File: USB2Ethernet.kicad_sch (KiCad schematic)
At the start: 23 parts, among them U15 LAN9512, U17 CAT250xxx, Y5 25Mhz

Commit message: change cad data
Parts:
- added C102, C97: 0.1uF, Capacitor_SMD:C_0402_1005Metric_Pad0.74x0.62mm_HandSolder, symbol Device:C
- added FB4: FerriteBead, Inductor_SMD:L_0603_1608Metric_Pad1.05x0.95mm_HandSolder, symbol Device:FerriteBead
- added R54, R55, R56, R57: 49.9Ω, Resistor_SMD:R_0603_1608Metric_Pad0.98x0.95mm_HandSolder, symbol Device:R
- added R59, R61: 12kΩ, Resistor_SMD:R_0603_1608Metric_Pad0.98x0.95mm_HandSolder, symbol Device:R
- added R63: 1k, Resistor_SMD:R_0603_1608Metric_Pad0.98x0.95mm_HandSolder, symbol Device:R
- R64: renamed from R46; value 320kΩ -> 10kΩ
- Y6: renamed from Y5; footprint Crystal:Crystal_SMD_SeikoEpson_FA238-4Pin_3.2x2.5mm -> Crystal:Crystal_SMD_SeikoEpson_FA128-4Pin_2.0x1.6mm
- renumbered C84 to C111, C86 to C112, C92 to C113, C93 to C122, C98 to C123, C99 to C124, C100 to C128, C105 to C129, C109 to C131, C110 to C132, C112 to C134, C64 to C86, C69 to C88, C72 to C92, C73 to C93, C71 to C94, C70 to C95, C68 to C96, FB2 to FB5, U15 to U16, U17 to U18
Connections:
- net +3.3V: now also U16.41 (AUTOMDIX_EN), R54.1, R55.1, R56.1, R57.1, R63.1
- net 1.8V: no longer U16.48 (VDD18ETHPLL)
- net GND: now also R59.1, R61.1
- net RXN: now also R54.2
- net RXP: now also R55.2
- net TXN: now also R56.2
- net TXP: now also R57.2
- net at U16.62 (VDD18USBPLL): now also C97.2
- net at U16.11 (VBUS_DET): now also R63.2
- net USB2DM: now reaches U16.3 (USBDM3)
- net USB2DP: now reaches U16.4 (USBDP3)
- net at U16.50 (EXRES): now also R59.2
- net at U16.63 (USBRBIAS): now also R61.2
- new net: C102.2, U16.48 (VDD18ETHPLL)
- new net: C102.1, FB4.1
- new net: C97.1, FB4.2
- no-connect marks 0 -> 12
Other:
- moved on the sheet: C111, C112, C113, C122, C123, C124, C128, C129, C131, C132, C134, C86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

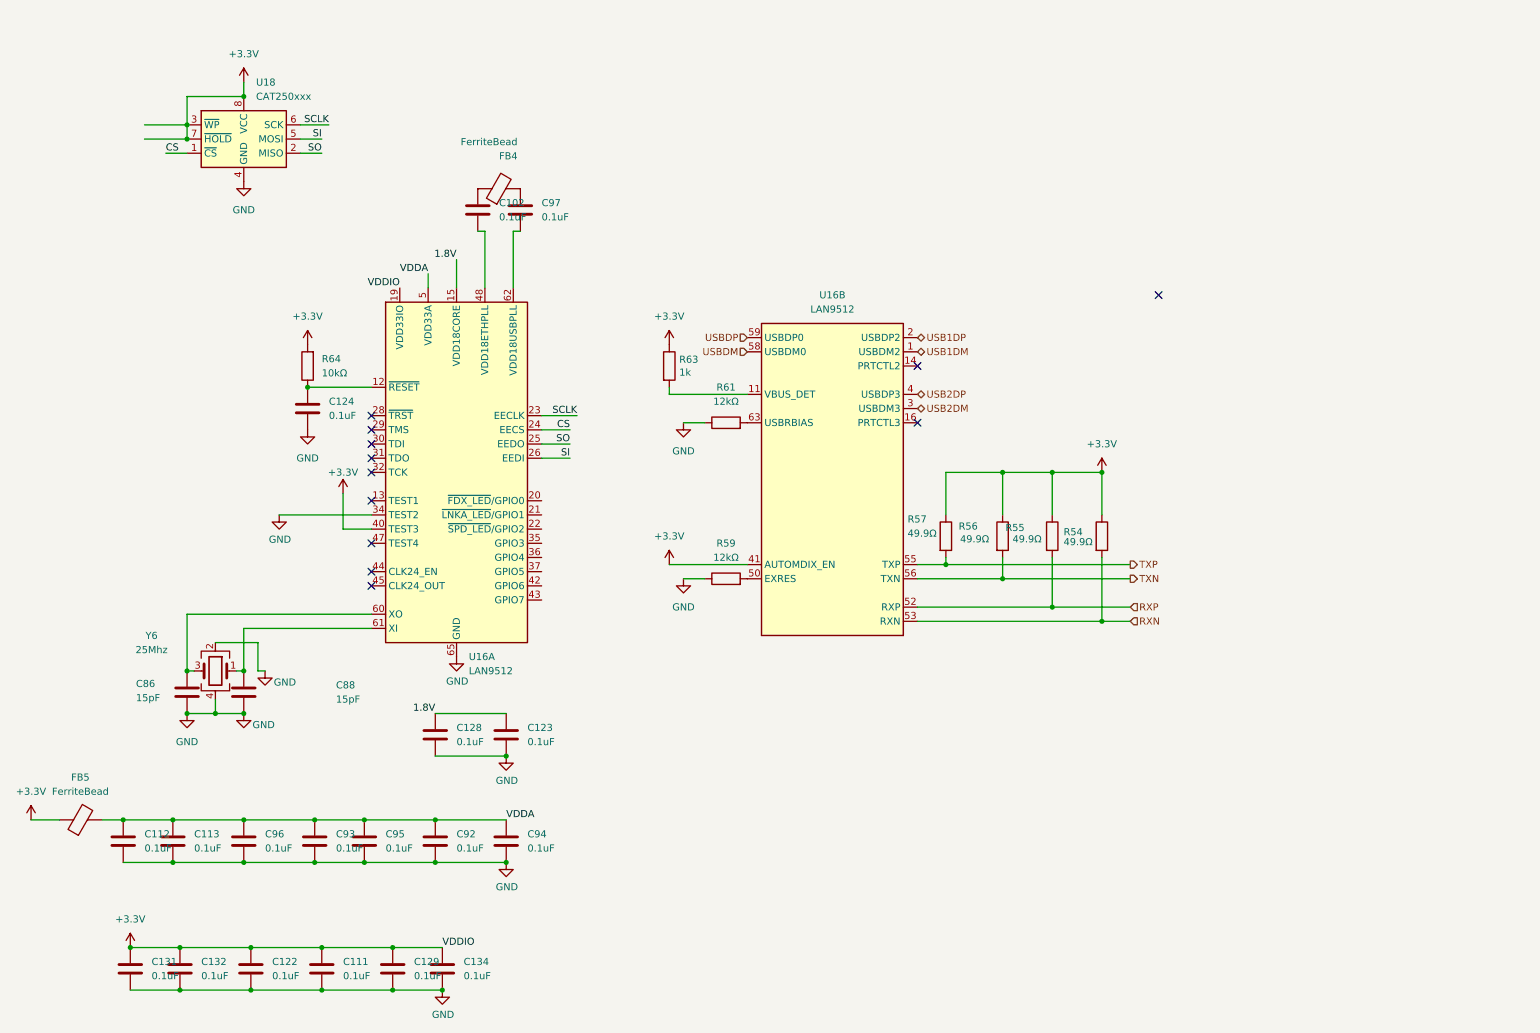
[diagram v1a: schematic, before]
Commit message: remove efuse
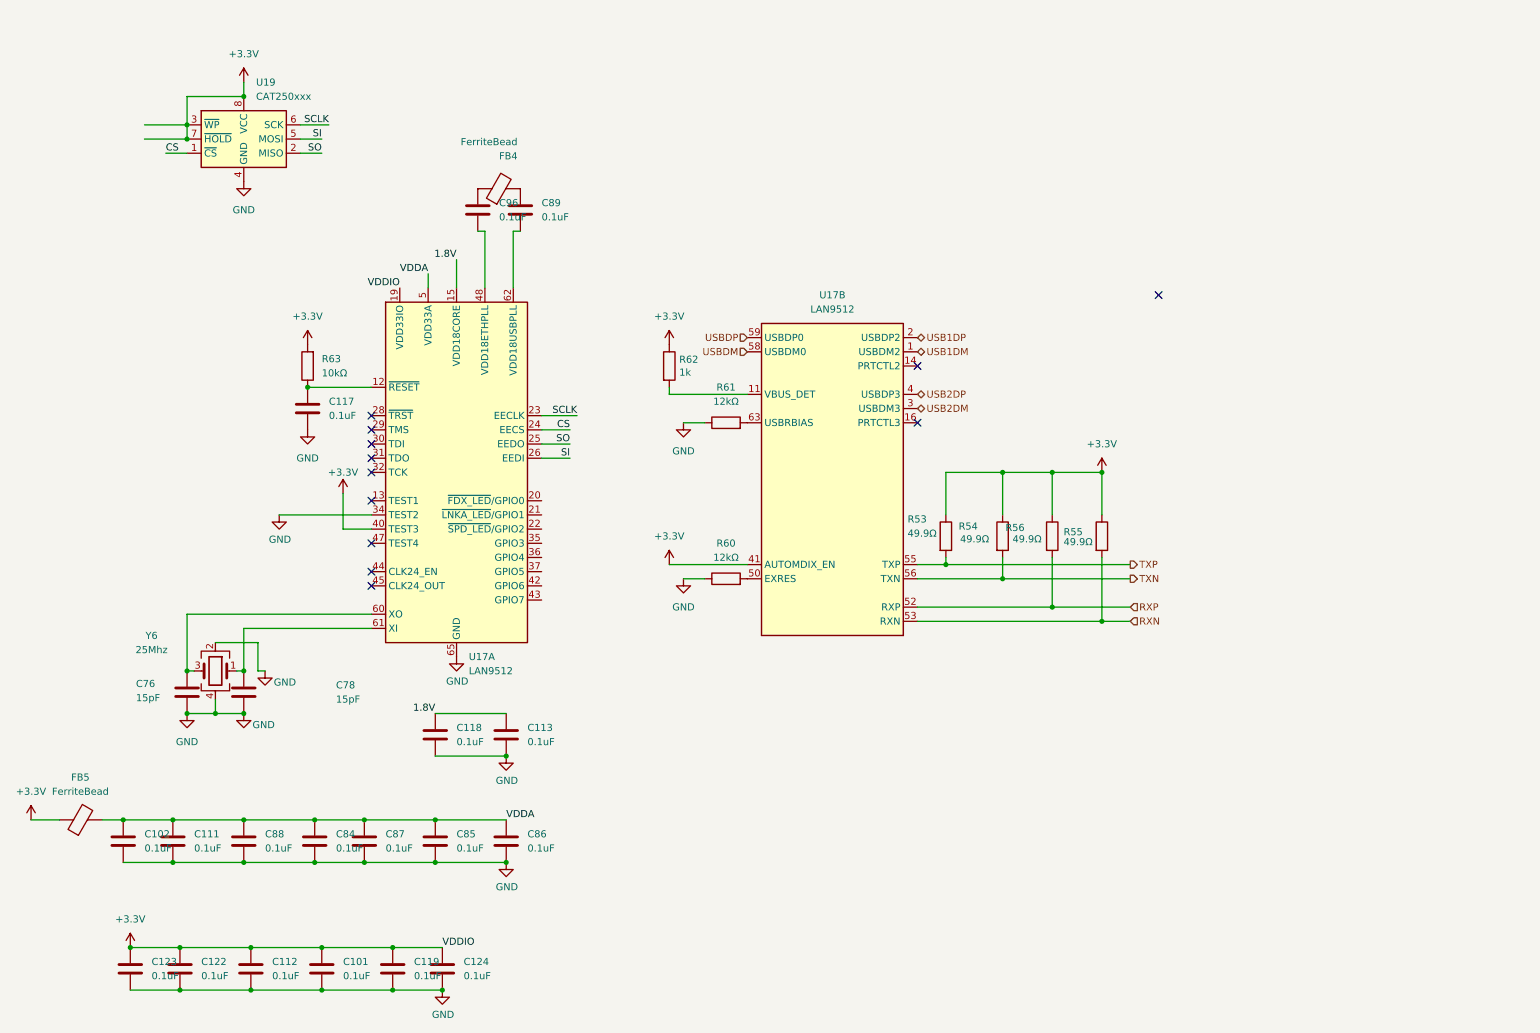
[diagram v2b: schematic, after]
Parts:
- renumbered C111 to C101, C112 to C102, C113 to C111, C122 to C112, C123 to C113, C124 to C117, C128 to C118, C129 to C119, C132 to C122, C131 to C123, C134 to C124, C86 to C76, C88 to C78, C93 to C84, C92 to C85, C94 to C86, C95 to C87, C96 to C88, C97 to C89, C102 to C96, R57 to R53, R56 to R54, R54 to R55, R55 to R56, R59 to R60, R63 to R62, R64 to R63, U16 to U17, U18 to U19
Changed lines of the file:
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@@
 		(dnp no)
 		(fields_autoplaced yes)
-		(property "Reference" "C94"
+		(property "Reference" "C86"
 			(at 104.14 166.3699 0)
 			(effects
@@
 			(project "mainboard4"
 				(path "/dd07ab80-a59c-44f4-ac7d-849e21e1384e/3546f414-4018-45c7-a00a-bf02d214bf7f"
-					(reference "C94")
+					(reference "C86")
 					(unit 1)
 				)
@@
 		(dnp no)
 		(fields_autoplaced yes)
-		(property "Reference" "C132"
+		(property "Reference" "C122"
 			(at 45.72 189.2299 0)
 			(effects
@@
 			(project "mainboard4"
 				(path "/dd07ab80-a59c-44f4-ac7d-849e21e1384e/3546f414-4018-45c7-a00a-bf02d214bf7f"
-					(reference "C132")
+					(reference "C122")
 					(unit 1)
 				)
@@
 		(dnp no)
 		(fields_autoplaced yes)
-		(property "Reference" "C92"
+		(property "Reference" "C85"
 			(at 91.44 166.3699 0)
 			(effects
@@
 			(project "mainboard4"
 				(path "/dd07ab80-a59c-44f4-ac7d-849e21e1384e/3546f414-4018-45c7-a00a-bf02d214bf7f"
-					(reference "C92")
+					(reference "C85")
 					(unit 1)
 				)
@@
 		(on_board yes)
 		(dnp no)
-		(property "Reference" "C86"
+		(property "Reference" "C76"
 			(at 34.036 139.446 0)
 			(effects
@@
 			(project "mainboard4"
 				(path "/dd07ab80-a59c-44f4-ac7d-849e21e1384e/3546f414-4018-45c7-a00a-bf02d214bf7f"
-					(reference "C86")
+					(reference "C76")
 					(unit 1)
 				)
@@
 		(on_board yes)
 		(dnp no)
-		(property "Reference" "R54"
+		(property "Reference" "R55"
 			(at 200.152 112.268 0)
 			(effects
@@
 			(project "mainboard4"
 				(path "/dd07ab80-a59c-44f4-ac7d-849e21e1384e/3546f414-4018-45c7-a00a-bf02d214bf7f"
-					(reference "R54")
+					(reference "R55")
 					(unit 1)
 				)
@@
 		(dnp no)
 		(fields_autoplaced yes)
-		(property "Reference" "C124"
+		(property "Reference" "C117"
 			(at 68.58 88.8999 0)
 			(effects
@@
 			(project "mainboard4"
 				(path "/dd07ab80-a59c-44f4-ac7d-849e21e1384e/3546f414-4018-45c7-a00a-bf02d214bf7f"
-					(reference "C124")
+					(reference "C117")
 					(unit 1)
 				)
@@
 		(dnp no)
 		(fields_autoplaced yes)
-		(property "Reference" "U16"
+		(property "Reference" "U17"
 			(at 93.6341 134.62 0)
 			(effects
@@
 			(project ""
 				(path "/dd07ab80-a59c-44f4-ac7d-849e21e1384e/3546f414-4018-45c7-a00a-bf02d214bf7f"
-					(reference "U16")
+					(reference "U17")
 					(unit 1)
 				)
@@
 		(dnp no)
 		(fields_autoplaced yes)
-		(property "Reference" "R64"
+		(property "Reference" "R63"
 			(at 67.31 81.2799 0)
 			(effects
@@
 			(project "mainboard4"
 				(path "/dd07ab80-a59c-44f4-ac7d-849e21e1384e/3546f414-4018-45c7-a00a-bf02d214bf7f"
-					(reference "R64")
+					(reference "R63")
 					(unit 1)
 				)
@@
 		(dnp no)
 		(fields_autoplaced yes)
-		(property "Reference" "C95"
+		(property "Reference" "C87"
 			(at 78.74 166.3699 0)
 			(effects
@@
 			(project "mainboard4"
 				(path "/dd07ab80-a59c-44f4-ac7d-849e21e1384e/3546f414-4018-45c7-a00a-bf02d214bf7f"
-					(reference "C95")
+					(reference "C87")
 					(unit 1)
 				)
@@
 		(on_board yes)
 		(dnp no)
-		(property "Reference" "R56"
+		(property "Reference" "R54"
 			(at 181.356 111.252 0)
 			(effects
@@
 			(project "mainboard4"
 				(path "/dd07ab80-a59c-44f4-ac7d-849e21e1384e/3546f414-4018-45c7-a00a-bf02d214bf7f"
-					(reference "R56")
+					(reference "R54")
 					(unit 1)
 				)
@@
 		(dnp no)
 		(fields_autoplaced yes)
-		(property "Reference" "U18"
+		(property "Reference" "U19"
 			(at 55.5341 31.75 0)
 			(effects
@@
 			(project "mainboard4"
 				(path "/dd07ab80-a59c-44f4-ac7d-849e21e1384e/3546f414-4018-45c7-a00a-bf02d214bf7f"
-					(reference "U18")
+					(reference "U19")
 					(unit 1)
 				)
@@
 		(dnp no)
 		(fields_autoplaced yes)
-		(property "Reference" "C102"
+		(property "Reference" "C96"
 			(at 99.06 53.3399 0)
 			(effects
@@
 			(project "mainboard4"
 				(path "/dd07ab80-a59c-44f4-ac7d-849e21e1384e/3546f414-4018-45c7-a00a-bf02d214bf7f"
-					(reference "C102")
+					(reference "C96")
 					(unit 1)
 				)
@@
 		(dnp no)
 		(fields_autoplaced yes)
-		(property "Reference" "C122"
+		(property "Reference" "C112"
 			(at 58.42 189.2299 0)
 			(effects
@@
 			(project "mainboard4"
 				(path "/dd07ab80-a59c-44f4-ac7d-849e21e1384e/3546f414-4018-45c7-a00a-bf02d214bf7f"
-					(reference "C122")
+					(reference "C112")
 					(unit 1)
 				)
@@
 		(on_board yes)
 		(dnp no)
-		(property "Reference" "R57"
+		(property "Reference" "R53"
 			(at 172.212 109.982 0)
 			(effects
@@
 			(project "mainboard4"
 				(path "/dd07ab80-a59c-44f4-ac7d-849e21e1384e/3546f414-4018-45c7-a00a-bf02d214bf7f"
-					(reference "R57")
+					(reference "R53")
 					(unit 1)
 				)
@@
 		(dnp no)
 		(fields_autoplaced yes)
-		(property "Reference" "C111"
+		(property "Reference" "C101"
 			(at 71.12 189.2299 0)
 			(effects
@@
 			(project "mainboard4"
 				(path "/dd07ab80-a59c-44f4-ac7d-849e21e1384e/3546f414-4018-45c7-a00a-bf02d214bf7f"
-					(reference "C111")
+					(reference "C101")
 					(unit 1)
 				)
@@
 		(on_board yes)
 		(dnp no)
-		(property "Reference" "R55"
+		(property "Reference" "R56"
 			(at 189.738 111.506 0)
 			(effects
@@
 			(project "mainboard4"
 				(path "/dd07ab80-a59c-44f4-ac7d-849e21e1384e/3546f414-4018-45c7-a00a-bf02d214bf7f"
-					(reference "R55")
+					(reference "R56")
 					(unit 1)
 				)
@@
 		(dnp no)
 		(fields_autoplaced yes)
-		(property "Reference" "U16"
+		(property "Reference" "U17"
 			(at 158.75 69.85 0)
 			(effects
@@
 			(project ""
 				(path "/dd07ab80-a59c-44f4-ac7d-849e21e1384e/3546f414-4018-45c7-a00a-bf02d214bf7f"
-					(reference "U16")
+					(reference "U17")
 					(unit 2)
 				)
@@
 		(dnp no)
 		(fields_autoplaced yes)
-		(property "Reference" "C128"
+		(property "Reference" "C118"
 			(at 91.44 147.3199 0)
 			(effects
@@
 			(project "mainboard4"
 				(path "/dd07ab80-a59c-44f4-ac7d-849e21e1384e/3546f414-4018-45c7-a00a-bf02d214bf7f"
-					(reference "C128")
+					(reference "C118")
 					(unit 1)
 				)
@@
 		(dnp no)
 		(fields_autoplaced yes)
-		(property "Reference" "C131"
+		(property "Reference" "C123"
 			(at 36.83 189.2299 0)
 			(effects
@@
 			(project "mainboard4"
 				(path "/dd07ab80-a59c-44f4-ac7d-849e21e1384e/3546f414-4018-45c7-a00a-bf02d214bf7f"
-					(reference "C131")
+					(reference "C123")
 					(unit 1)
 				)
@@
 		(dnp no)
 		(fields_autoplaced yes)
-		(property "Reference" "C129"
+		(property "Reference" "C119"
 			(at 83.82 189.2299 0)
 			(effects
@@
 			(project "mainboard4"
 				(path "/dd07ab80-a59c-44f4-ac7d-849e21e1384e/3546f414-4018-45c7-a00a-bf02d214bf7f"
-					(reference "C129")
+					(reference "C119")
 					(unit 1)
 				)
@@
 		(dnp no)
 		(fields_autoplaced yes)
-		(property "Reference" "C96"
+		(property "Reference" "C88"
 			(at 57.15 166.3699 0)
 			(effects
@@
 			(project "mainboard4"
 				(path "/dd07ab80-a59c-44f4-ac7d-849e21e1384e/3546f414-4018-45c7-a00a-bf02d214bf7f"
-					(reference "C96")
+					(reference "C88")
 					(unit 1)
 				)
@@
 		(dnp no)
 		(fields_autoplaced yes)
-		(property "Reference" "C93"
+		(property "Reference" "C84"
 			(at 69.85 166.3699 0)
 			(effects
@@
 			(project "mainboard4"
 				(path "/dd07ab80-a59c-44f4-ac7d-849e21e1384e/3546f414-4018-45c7-a00a-bf02d214bf7f"
-					(reference "C93")
+					(reference "C84")
 					(unit 1)
 				)
@@
 		(dnp no)
 		(fields_autoplaced yes)
-		(property "Reference" "R59"
+		(property "Reference" "R60"
 			(at 139.7 114.3 90)
 			(effects
@@
 			(project "mainboard4"
 				(path "/dd07ab80-a59c-44f4-ac7d-849e21e1384e/3546f414-4018-45c7-a00a-bf02d214bf7f"
-					(reference "R59")
+					(reference "R60")
 					(unit 1)
 				)
@@
 		(on_board yes)
 		(dnp no)
-		(property "Reference" "C88"
+		(property "Reference" "C78"
 			(at 69.85 139.6999 0)
 			(effects
@@
 			(project "mainboard4"
 				(path "/dd07ab80-a59c-44f4-ac7d-849e21e1384e/3546f414-4018-45c7-a00a-bf02d214bf7f"
-					(reference "C88")
+					(reference "C78")
 					(unit 1)
 				)
@@
 		(dnp no)
 		(fields_autoplaced yes)
-		(property "Reference" "C123"
+		(property "Reference" "C113"
 			(at 104.14 147.3199 0)
 			(effects
@@
 			(project "mainboard4"
 				(path "/dd07ab80-a59c-44f4-ac7d-849e21e1384e/3546f414-4018-45c7-a00a-bf02d214bf7f"
-					(reference "C123")
+					(reference "C113")
 					(unit 1)
 				)
@@
 		(dnp no)
 		(fields_autoplaced yes)
-		(property "Reference" "C112"
+		(property "Reference" "C102"
 			(at 35.56 166.3699 0)
 			(effects
@@
 			(project "mainboard4"
 				(path "/dd07ab80-a59c-44f4-ac7d-849e21e1384e/3546f414-4018-45c7-a00a-bf02d214bf7f"
-					(reference "C112")
+					(reference "C102")
 					(unit 1)
 				)
@@
 		(dnp no)
 		(fields_autoplaced yes)
-		(property "Reference" "C113"
+		(property "Reference" "C111"
 			(at 44.45 166.3699 0)
 			(effects
@@
 			(project "mainboard4"
 				(path "/dd07ab80-a59c-44f4-ac7d-849e21e1384e/3546f414-4018-45c7-a00a-bf02d214bf7f"
-					(reference "C113")
+					(reference "C111")
 					(unit 1)
 				)
@@
 		(dnp no)
 		(fields_autoplaced yes)
-		(property "Reference" "C134"
+		(property "Reference" "C124"
 			(at 92.71 189.2299 0)
 			(effects
@@
 			(project "mainboard4"
 				(path "/dd07ab80-a59c-44f4-ac7d-849e21e1384e/3546f414-4018-45c7-a00a-bf02d214bf7f"
-					(reference "C134")
+					(reference "C124")
 					(unit 1)
 				)
@@
 		(dnp no)
 		(fields_autoplaced yes)
-		(property "Reference" "C97"
+		(property "Reference" "C89"
 			(at 106.68 53.3399 0)
 			(effects
@@
 			(project "mainboard4"
 				(path "/dd07ab80-a59c-44f4-ac7d-849e21e1384e/3546f414-4018-45c7-a00a-bf02d214bf7f"
-					(reference "C97")
+					(reference "C89")
 					(unit 1)
 				)
@@
 		(on_board yes)
 		(dnp no)
-		(property "Reference" "R63"
+		(property "Reference" "R62"
 			(at 131.318 81.3816 0)
 			(effects
@@
 			(project "mainboard4"
 				(path "/dd07ab80-a59c-44f4-ac7d-849e21e1384e/3546f414-4018-45c7-a00a-bf02d214bf7f"
-					(reference "R63")
+					(reference "R62")
 					(unit 1)
 				)

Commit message: change design
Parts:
- added R68, R69: 10kΩ, Resistor_SMD:R_0603_1608Metric_Pad0.98x0.95mm_HandSolder, symbol Device:R
- C117: value 0.1uF -> 0.01uF
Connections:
- net +3.3V: now also R69.1; no longer R53.1, R54.1, R55.1, R56.1, U17.41 (AUTOMDIX_EN)
- net CS: now also R68.2
- net GND: now also R68.1
- net VDDA: now also R53.1, R54.1, R55.1, R56.1
- new net: R69.2, U17.41 (AUTOMDIX_EN)
- no-connect marks 12 -> 11
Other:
- moved on the sheet: C101, C102, C111, C112, C113, C117, C118, C119, C122, C123, C124, C76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
